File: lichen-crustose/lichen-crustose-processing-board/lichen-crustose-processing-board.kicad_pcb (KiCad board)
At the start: 2 copper layers, 48 x 108 mm, 25 parts, among them U1 LM4040-2.5

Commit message: Updates Lichen symbols and footprints. Fixes to Crustose and Vactrol VCA. Adds 3D model of the RP2350 dual USB board.
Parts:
- added H3: MountingHole_Pad, MountingHole:MountingHole_2.2mm_M2_Pad, F.Cu at (117.0, 117.0)
- moved TR4 14.5 mm to (145.4, 163.8), turned to 180 degrees
- moved LED8 5.30 mm to (127.8, 162.5), turned to 90 degrees
- moved LED2 5.00 mm to (127.5, 172.2), turned to 90 degrees
- moved LED5 5.00 mm to (122.5, 172.2), turned to 90 degrees
- moved LED6 5.00 mm to (122.5, 162.5), turned to 90 degrees
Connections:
- TR4 pad 1: Net-(LED5-K) -> /RM_L_SOCKET
- TR4 pad 2: GND -> unconnected-(TR4-Pad2)
- TR4 pad 3: Net-(LED2-A) -> GND
- TR4 pad 4: GND -> Net-(LED2-A)
- TR4 pad 5: unconnected-(TR4-Pad5) -> GND
- TR4 pad 6: /RM_L_SOCKET -> Net-(LED5-K)
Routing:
- net /RM_L_SOCKET: track 65.3 -> 58.1 mm
- net Net-(LED5-K): track 14.5 -> 20.3 mm
- net Net-(LED2-A): track 20.7 -> 15.6 mm
- net /CARRER_L_SOCKET: track 28.4 -> 29.8 mm

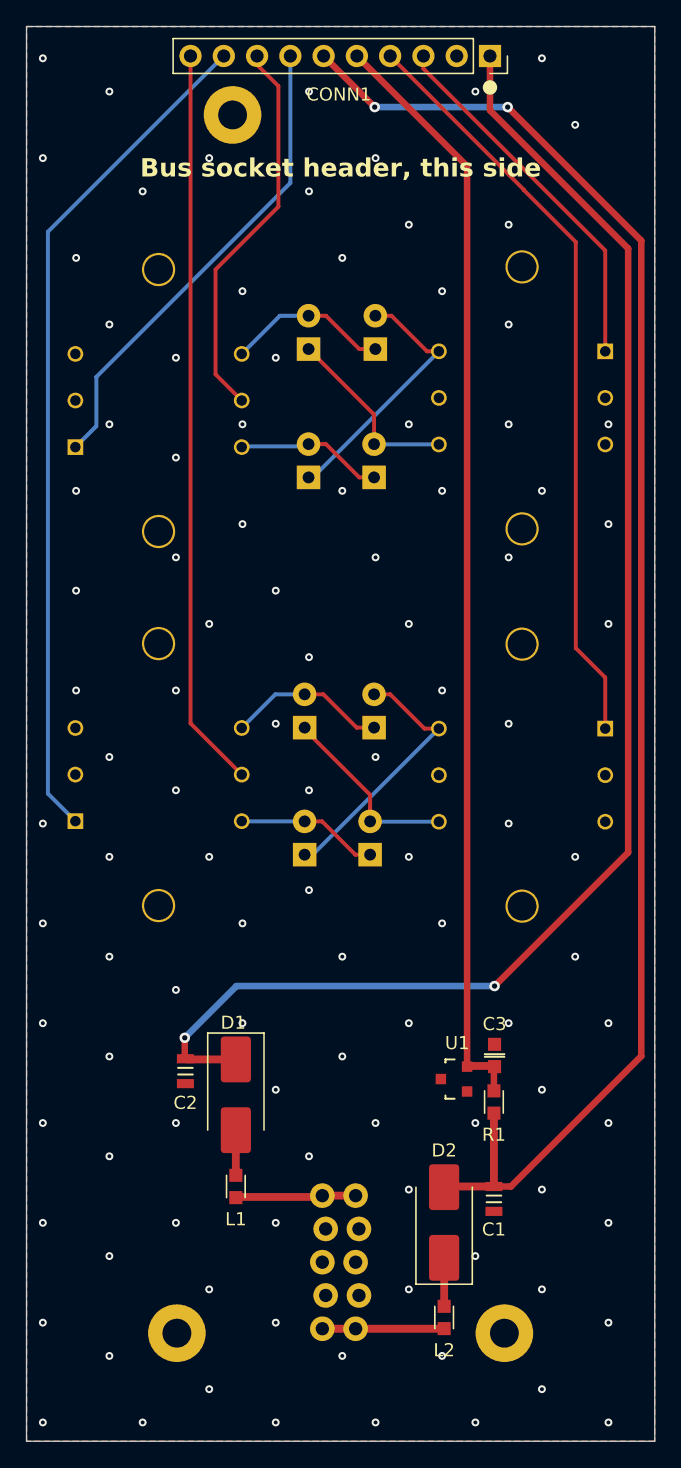
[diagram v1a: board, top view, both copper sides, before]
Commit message: feat: Updates Crustose, Cladonia and YouMe Transformer. Adds Stereo Latencies.
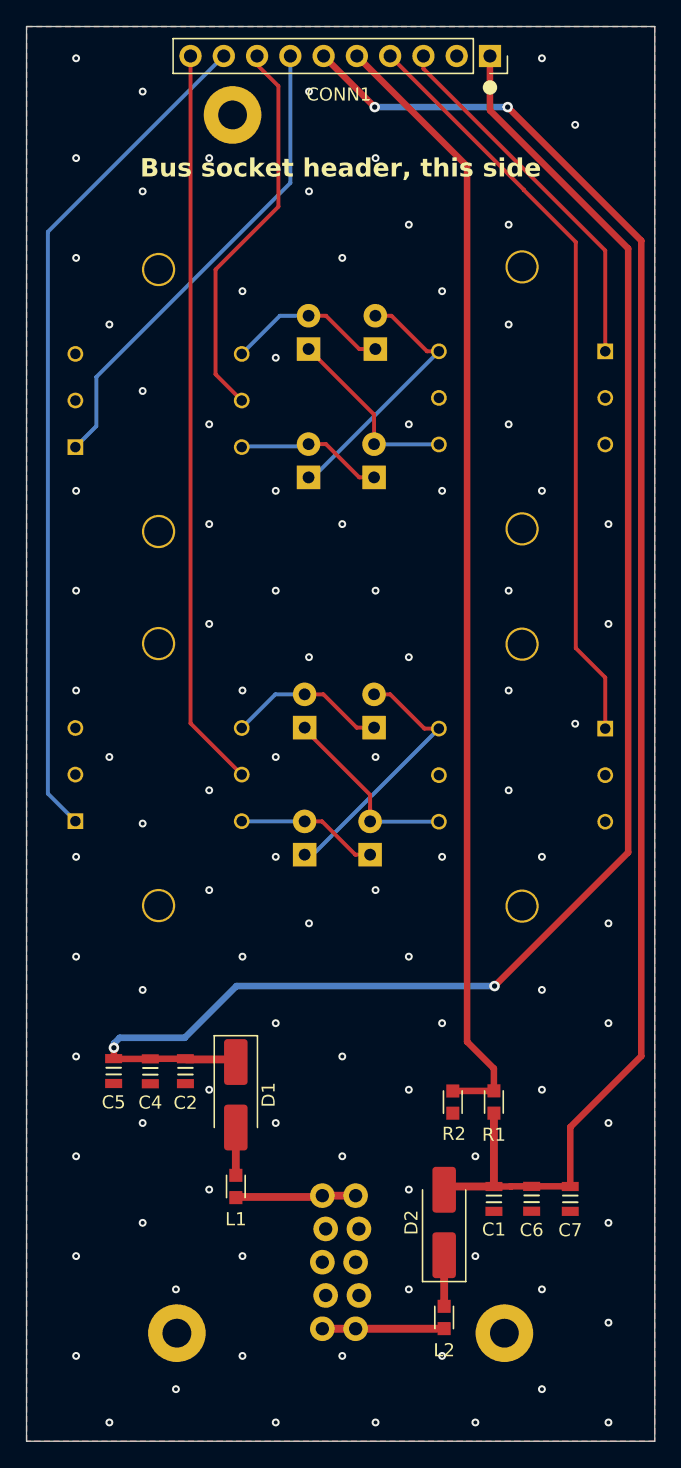
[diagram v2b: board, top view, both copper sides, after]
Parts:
- removed C3: 100nF_0603_50V, Lichen:C_0603
- removed U1: LM4040-2.5, PCM_4ms_Package_SOT:SOT23-3_PO132
- added C4: 10uF, Lichen:C_0805, F.Cu at (110.7, 190.0)
- added C5: 10uF, Lichen:C_0805, F.Cu at (107.9, 190.0)
- added C6: 10uF, Lichen:C_0805, F.Cu at (139.8, 199.7)
- added C7: 10uF, Lichen:C_0805, F.Cu at (142.8, 199.8)
- added R2: 10K, Lichen:R_0603, F.Cu at (133.8, 192.4)
- C1, C2: value 10uF_0805_25V -> 10uF
- D1, D2: footprint Diode_SMD:D_SMB_Handsoldering -> Diode_SMD:D_SMA_Handsoldering
- R1: value 470R_0603 -> 39K
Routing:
- net +12V: track 110.4 -> 121.1 mm
- net -12V: track 117.1 -> 119.8 mm
- net -2.5V: track 84.6 -> 86.5 mm
- net GND: vias 106 -> 97
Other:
- board text added: "v1.1 © 2026, Colin Clark"
- board text removed: "v1.0 © 2025, Colin Clark"
